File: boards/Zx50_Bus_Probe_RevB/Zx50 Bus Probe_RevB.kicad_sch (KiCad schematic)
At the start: 81 parts, among them J1 Zx50_EdgeConnector, J10 CH1, J11 CH2, J12 CH3, J13 DISPL SOCKET, J14 DISPL SOCKET, J15 Z80_Addr, J16 Z80_Data, J17 Z80_Ctrl, J18 Clock, J19 SH_Data, J2 OUT, J20 SH_Ctrl, J3 IN, J4 PIC PGM, J5 P0, J6 P1, J7 P2, J8 Send/Recv Card, J9 CH0, U1 MCP23S17_SP, U10 CD74HC4051E, U11 CD74HC4051E, U12 CD74HC4051E, U13 MCP23S17_SP, U14 CD74HC154M96, U15 OPA356xxD, U16 OPA356xxD, U17 PIC18F4620-I_P, U18 74AHCT541, U19 Jumper, U2 CD74HC4051E, U20 Jumper, U21 Jumper, U22 Jumper, U23 Jumper, U24 Jumper, U25 Jumper, U3 CD74HC4051E, U4 CD74HC4051E, U5 CD74HC4051E, U6 SN74ABT245BN, U7 SN74ABT245BN, U8 CD74HC4051E, U9 CD74HC4051E

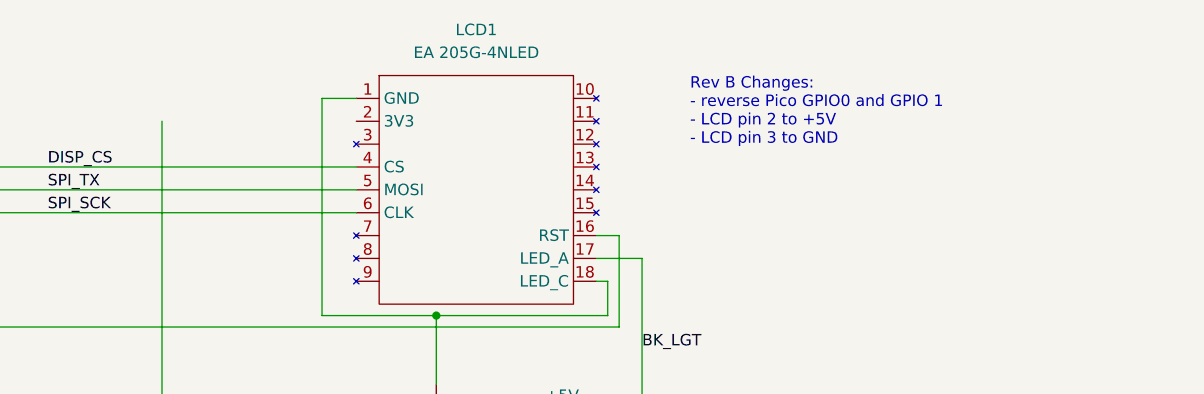
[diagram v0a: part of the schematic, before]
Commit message: enable wifi support for the bus probe
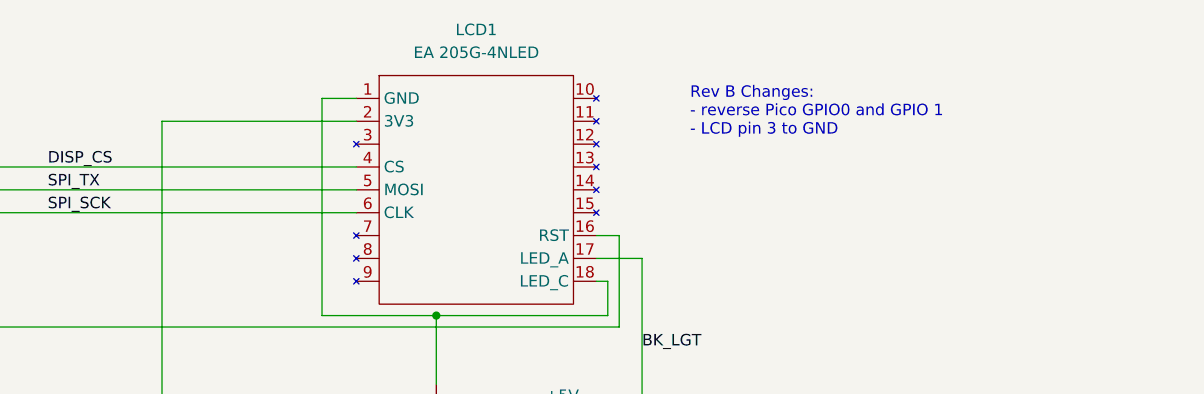
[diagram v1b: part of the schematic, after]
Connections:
- net at A1.36 (3V3): now also LCD1.2 (3V3)
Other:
- note added: "Rev B Changes: - reverse Pico GPIO0 and GPIO 1 - LCD pin 3 to GND"
- note removed: "Rev B Changes: - reverse Pico GPIO0 and GPIO 1 - LCD pin 2 to +5V - LCD pin 3 to GND"
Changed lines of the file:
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@@
 		)
 	)
-	(text "Rev B Changes:\n- reverse Pico GPIO0 and GPIO 1\n- LCD pin 2 to +5V\n- LCD pin 3 to GND"
+	(text "Rev B Changes:\n- reverse Pico GPIO0 and GPIO 1\n- LCD pin 3 to GND"
 		(exclude_from_sim yes)
 		(at 113.284 26.924 0)
@@
 		)
 		(stroke
+			(width 0)
+			(type default)
+		)
+	)
+	(wire
+		(pts
+			(xy 54.61 27.94) (xy 76.2 27.94)
+		)
+		(stroke

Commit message: Add extra banners and such to tcp server.  updates to revb bus probe.
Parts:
- added R20: 3.3K, Potentiometer_THT:Potentiometer_Runtron_RM-063_Horizontal, symbol Device:R_Potentiometer_Trim
- C21: value 10uF -> 47uF
- U10, U11, U12, U3, U4, U5, U8, U9: now fitted
- U15: renamed from U16; Digi-Key_PN 296-12407-5-ND -> 296-12407-5-ND
- U16: renamed from U15; Digi-Key_PN 296-12407-5-ND -> 296-12407-5-ND
- U2: Digi-Key_PN 296-12810-5-ND -> 296-12810-5-ND; now fitted
- renumbered C19 to C18, C18 to C19, C4 to C3, C3 to C4, J3 to J2, J2 to J3, U19 to J80, U20 to J81, U21 to J82, U22 to J83, U23 to J84, U24 to J85, U25 to J86, J13 to J90, J14 to J91
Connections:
- net +5V: now also A1.39 (VSYS)
- net GND: now also R20.1
- net PICO_TX: now reaches A1.1 (GPIO0), U18.2 (A0)
- net PICO_RX: now reaches A1.2 (GPIO1), R5.1, R6.2
- net at A1.36 (3V3), LCD1.2 (3V3): now also R20.3
- net at LCD1.3 (Contrast): now also R20.2
- no-connect marks 52 -> 51
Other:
- note added: "Rev B Changes: - reverse Pico GPIO0 and GPIO 1 - LCD pin 3 to contrast adjustment - Pico pin 39 (Vsys) to +5V"
- note removed: "Rev B Changes: - reverse Pico GPIO0 and GPIO 1 - LCD pin 3 to GND"
- moved on the sheet: J90, J91

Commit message: updates for more robust tcp handing.
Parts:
- renumbered J3 to J2, J2 to J3, U16 to U15, U15 to U16
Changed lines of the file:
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@@
 		(on_board yes)
 		(dnp no)
-		(property "Reference" "J2"
+		(property "Reference" "J3"
 			(at 120.65 336.8431 0)
 			(effects
@@
 			(project "Zx50 Bus Probe_RevB"
 				(path "/25f447e7-64bf-42d9-acfb-0aea4b7e6169"
-					(reference "J2")
+					(reference "J3")
 					(unit 1)
 				)
@@
 		(dnp no)
 		(fields_autoplaced yes)
-		(property "Reference" "U16"
+		(property "Reference" "U15"
 			(at 156.7881 302.26 0)
 			(effects
@@
 			(project ""
 				(path "/25f447e7-64bf-42d9-acfb-0aea4b7e6169"
-					(reference "U16")
+					(reference "U15")
 					(unit 1)
 				)
@@
 		(on_board yes)
 		(dnp no)
-		(property "Reference" "U15"
+		(property "Reference" "U16"
 			(at 144.526 350.52 0)
 			(effects
@@
 			(project "Zx50 Bus Probe_RevB"
 				(path "/25f447e7-64bf-42d9-acfb-0aea4b7e6169"
-					(reference "U15")
+					(reference "U16")
 					(unit 1)
 				)
@@
 		(on_board yes)
 		(dnp no)
-		(property "Reference" "J3"
+		(property "Reference" "J2"
 			(at 119.38 311.4431 0)
 			(effects
@@
 			(project ""
 				(path "/25f447e7-64bf-42d9-acfb-0aea4b7e6169"
-					(reference "J3")
+					(reference "J2")
 					(unit 1)
 				)

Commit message: Many updates and board revisions.
- Backplane Rev D for better AC termination.
- BusProbe revision, much smaller card, use surface mount, faster multiplexers.
- Revised clock mezzanine to reduce ringing.
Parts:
- removed D1: MCLK, LED_THT:LED_D5.0mm_Horizontal_O1.27mm_Z3.0mm, symbol Device:LED
- removed D2: CLK, LED_THT:LED_D5.0mm_Horizontal_O1.27mm_Z3.0mm, symbol Device:LED
- removed J18: Clock, zx50_footprints:PinHeader_2x02_P2.54mm_Vertical_Row_Letter_Last, symbol Connector_Generic:Conn_02x02_Row_Letter_Last
- removed R7, R8: 2.2K, Resistor_THT:R_Axial_DIN0207_L6.3mm_D2.5mm_P5.08mm_Vertical, symbol Device:R
- removed U1, U13: MCP23S17_SP, Package_DIP:DIP-28_W7.62mm_Socket, symbol Interface_Expansion:MCP23S17_SP
- removed U10, U11, U12, U2, U3, U4, U5, U8, U9: CD74HC4051E, Package_DIP:DIP-16_W7.62mm_Socket, symbol 74xx:74HC4051
- removed U17: PIC18F4620-I_P, Package_DIP:DIP-40_W15.24mm_Socket, symbol zx50_symbols:PIC18F4620-I_P
- added C22, C23, C24, C25: .1uF, Capacitor_SMD:C_0805_2012Metric, symbol Device:C_Small
- added D4: 1N4001, Diode_THT:D_DO-41_SOD81_P10.16mm_Horizontal, symbol Diode:1N4001
- added D5: PIC, LED_THT:LED_D5.0mm_Horizontal_O1.27mm_Z3.0mm, symbol Device:LED
- added R11: 470, Resistor_THT:R_Axial_DIN0207_L6.3mm_D2.5mm_P5.08mm_Vertical, symbol Device:R
- added U1, U13, U21: MCP23S17_SO, Package_SO:SOIC-28W_7.5x17.9mm_P1.27mm, symbol Interface_Expansion:MCP23S17_SO
- added U10, U11, U12, U2, U3, U4, U5, U8, U9: 74CBT3251, Package_SO:SOIC-16_3.9x9.9mm_P1.27mm, symbol zx50_symbols:SN74CBT3251DR
- added U17, U19, U22, U23: SN74ABT245BN, zx50_footprints:NS20, symbol zx50_symbols:SN74ABT245BN
- added U20: PIC18F27Q43-I/SO, zx50_footprints:SOIC28_SO_MCH, symbol zx50_symbols:PIC18F27Q43-I_SO
- C1, C10, C11, C12, C13, C14, C15, C16, C17, C18, C19, C2, C20, C3, C4, C5, C6, C7, C8, C9: footprint Capacitor_THT:C_Disc_D5.0mm_W2.5mm_P2.50mm -> Capacitor_SMD:C_0805_2012Metric
- R2: footprint Resistor_THT:R_Axial_DIN0207_L6.3mm_D2.5mm_P10.16mm_Horizontal -> Resistor_SMD:R_0805_2012Metric_Pad1.20x1.40mm_HandSolder
- U18: footprint Package_DIP:DIP-20_W7.62mm_Socket -> Package_SO:SOIC-20W_7.5x12.8mm_P1.27mm; Digi-Key_PN 296-4755-5-ND -> 296-4754-1-ND
- U6, U7: footprint Package_DIP:DIP-20_W7.62mm_Socket -> zx50_footprints:NS20; Digi-Key_PN 296-3970-5-ND -> 296-15879-1-ND
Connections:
- net +5V: now also C20.1, C22.1, C23.1, C24.1, C25.1, D4.2 (A), D5.2 (A), U1.9 (VDD), U10.16 (VCC), U11.16 (VCC), U12.16 (VCC), U13.15 (A0), U13.9 (VDD), U17.20 (VCC), U19.20 (VCC), U2.16 (VCC), U20.20 (VDD), U21.16 (A1), U21.9 (VDD), U22.20 (VCC), U23.20 (VCC), U3.16 (VCC), U4.16 (VCC), U5.16 (VCC), U8.16 (VCC), U9.16 (VCC); no longer A1.39 (VSYS), C20.2
- net A0: now also U17.2 (A1), U4.12 (B8); no longer J15.1b (Pin_1b)
- net A1: now also U17.3 (A2), U4.4 (B1); no longer J15.2b (Pin_2b)
- net A10: now also U19.4 (A3), U5.13 (B7); no longer J15.11b (Pin_11b)
- net A11: now also U19.5 (A4), U5.3 (B2); no longer J15.12b (Pin_12b)
- net A12: now also U19.6 (A5), U5.14 (B6); no longer J15.13b (Pin_13b)
- net A13: now also U19.7 (A6), U5.2 (B3); no longer J15.14b (Pin_14b)
- net A14: now also U19.8 (A7), U5.15 (B5); no longer J15.15b (Pin_15b)
- net A15: now also U19.9 (A8), U5.1 (B4); no longer J15.16b (Pin_16b)
- net A2: now also U17.4 (A3), U4.13 (B7); no longer J15.3b (Pin_3b)
- net A3: now also U17.5 (A4), U4.3 (B2); no longer J15.4b (Pin_4b)
- net A4: now also U17.6 (A5), U4.14 (B6); no longer J15.5b (Pin_5b)
- net A5: now also U17.7 (A6), U4.2 (B3); no longer J15.6b (Pin_6b)
- net A6: now also U17.8 (A7), U4.15 (B5); no longer J15.7b (Pin_7b)
- net A7: now also U17.9 (A8), U4.1 (B4); no longer J15.8b (Pin_8b)
- net A8: now also U19.2 (A1), U5.12 (B8); no longer J15.9b (Pin_9b)
- net A9: now also U19.3 (A2), U5.4 (B1); no longer J15.10b (Pin_10b)
- net AN: now also U10.5 (A), U11.5 (A), U12.5 (A), U2.5 (A), U3.5 (A), U4.5 (A), U5.5 (A), U8.5 (A), U9.5 (A)
- net AUX: now also U20.25 (RB4)
- net CHIP0: now also U18.12 (Y6); no longer U18.17 (Y1)
- net CHIP1: now also U18.13 (Y5); no longer U18.16 (Y2)
- net CHIP2: now also U18.14 (Y4); no longer U18.15 (Y3)
- net CHIP3: now also U18.15 (Y3); no longer U18.14 (Y4)
- net CLK: now also U20.12 (RC1), U9.13 (B7)
- net D0: now also U3.12 (B8); no longer J16.1b (Pin_1b)
- net D1: now also U3.4 (B1); no longer J16.2b (Pin_2b)
- net D2: now also U3.13 (B7); no longer J16.3b (Pin_3b)
- net D3: now also U3.3 (B2); no longer J16.4b (Pin_4b)
- net D4: now also U3.14 (B6); no longer J16.5b (Pin_5b)
- net D5: now also U3.2 (B3); no longer J16.6b (Pin_6b)
- net D6: now also U3.15 (B5); no longer J16.7b (Pin_7b)
- net D7: now also U3.1 (B4); no longer J16.8b (Pin_8b)
- net G0: now also U11.4 (B1)
- net G1: now also U11.12 (B8)
- net G10: now also U12.3 (B2)
- net G11: now also U12.13 (B7)
- net G12: now also U12.2 (B3), U23.9 (A8)
- net G13: now also U12.14 (B6)
- net G14: now also U12.1 (B4), U23.7 (A6)
- net G15: now also U7.9 (A8), U12.15 (B5)
- net G2: now also U11.3 (B2)
- net G3: now also U11.13 (B7)
- net G4: now also U11.2 (B3)
- net G5: now also U11.14 (B6)
- net G6: now also U11.1 (B4)
- net G7: now also U11.15 (B5)
- net G8: now also U12.4 (B1)
- net G9: now also U12.12 (B8)
- net GND: now also C20.2, C22.2, C23.2, C24.2, C25.2, U1.10 (VSS), U1.15 (A0), U1.16 (A1), U1.17 (A2), U10.8 (GND), U11.8 (GND), U12.8 (GND), U13.10 (VSS), U13.16 (A1), U13.17 (A2), U17.10 (GND), U19.10 (GND), U2.8 (GND), U20.19 (VSS), U20.8 (VSS), U21.10 (VSS), U21.15 (A0), U21.17 (A2), U22.10 (GND), U23.10 (GND), U3.8 (GND), U4.8 (GND), U5.8 (GND), U8.8 (GND), U9.8 (GND); no longer C20.1
- net IEI: now also U9.4 (B1)
- net IEO: now also U9.3 (B2)
- net MCLK: now also U20.13 (RC2), U9.12 (B8)
- net MCLR_N: now also U20.1 (MCLR/VPP/RE3)
- net PGC: now also U20.27 (RB6/ICSPCLK)
- net PGD: now also U20.28 (RB7/ICSPDAT)
- net PICO_TX: now also U18.9 (A7); no longer U18.2 (A0)
- net PORT0: now also U18.16 (Y2), U10.11 (S0), U11.11 (S0), U12.11 (S0), U2.11 (S0), U3.11 (S0), U4.11 (S0), U5.11 (S0), U8.11 (S0), U9.11 (S0); no longer U18.13 (Y5)
- net PORT1: now also U18.17 (Y1), U10.10 (S1), U11.10 (S1), U12.10 (S1), U2.10 (S1), U3.10 (S1), U4.10 (S1), U5.10 (S1), U8.10 (S1), U9.10 (S1); no longer U18.12 (Y6)
- net PORT2: now also U18.18 (Y0), U10.9 (S2), U11.9 (S2), U12.9 (S2), U2.9 (S2), U3.9 (S2), U4.9 (S2), U5.9 (S2), U8.9 (S2), U9.9 (S2); no longer U18.11 (Y7)
- net RA0: now also U6.19 (*OE), U20.2 (RA0); no longer U7.19 (*OE)
- net RA1: now also U6.1 (DIR), U20.3 (RA1); no longer U7.1 (DIR)
- net RA2: now also U7.19 (*OE), U17.19 (*OE), U19.19 (*OE), U20.4 (RA2); no longer U6.19 (*OE)
- net RA3: now also U7.1 (DIR), U17.1 (DIR), U19.1 (DIR), U20.5 (RA3); no longer U6.1 (DIR)
- net RA4: now also U1.18 (~{RESET}), U13.18 (~{RESET}), U20.6 (RA4), U21.18 (~{RESET})
- net RA5: now also U1.11 (~{CS}), U13.11 (~{CS}), U20.7 (RA5), U21.11 (~{CS})
- net RB5: now also R11.1, U20.26 (RB5); no longer J4.6 (Pin_6), U7.18 (B1)
- net RX: now also U18.11 (Y7), U20.18 (RC7); no longer U18.18 (Y0)
- net SCK: now also U1.12 (SCK), U13.12 (SCK), U20.14 (RC3), U21.12 (SCK)
- net SD0: now also U10.12 (B8), U22.2 (A1); no longer J19.1b (Pin_1b)
- net SD1: now also U10.4 (B1), U22.3 (A2); no longer J19.2b (Pin_2b)
- net SD2: now also U10.13 (B7), U22.4 (A3); no longer J19.3b (Pin_3b)
- net SD3: now also U10.3 (B2), U22.5 (A4); no longer J19.4b (Pin_4b)
- net SD4: now also U10.14 (B6), U22.6 (A5); no longer J19.5b (Pin_5b)
- net SD5: now also U10.2 (B3), U22.7 (A6); no longer J19.6b (Pin_6b)
- net SD6: now also U10.15 (B5), U22.8 (A7); no longer J19.7b (Pin_7b)
- net SD7: now also U10.1 (B4), U22.9 (A8); no longer J19.8b (Pin_8b)
- net SDI: now also U1.14 (SO), U13.14 (SO), U20.15 (RC4), U21.14 (SO)
- net SDO: now also U1.13 (SI), U13.13 (SI), U20.16 (RC5), U21.13 (SI)
- net SEL0: now also U3.7 (*OE)
- net SEL1: now also U2.7 (*OE)
- net SEL2: now also U12.7 (*OE)
- net SEL3: now also U11.7 (*OE)
- net SEL4: now also U4.7 (*OE)
- net SEL5: now also U5.7 (*OE)
- net SEL6: now also U10.7 (*OE)
- net SEL7: now also U8.7 (*OE)
- net SEL8: now also U9.7 (*OE)
- net SH_RW: now also U23.5 (A4), U9.1 (B4); no longer J20.4b (Pin_4b)
- net TX: now also U20.17 (RC6)
- net ~BUSAK~: now also U7.8 (A7), U8.15 (B5)
- net ~BUSRQ~: now also U20.24 (RB3), U8.2 (B3)
- net ~HALT~: now also U8.13 (B7)
- net ~INT~: now also U20.21 (RB0), U8.1 (B4)
- net ~IORQ~: now also U2.3 (B2); no longer J17.4b (Pin_4b)
- net ~M1~: now also U2.14 (B6); no longer J17.5b (Pin_5b)
- net ~MREQ~: now also U2.13 (B7); no longer J17.3b (Pin_3b)
- net ~NMI~: now also U2.1 (B4)
- net ~RD~: now also U2.12 (B8); no longer J17.1b (Pin_1b)
- net ~RESET~: now also U8.4 (B1); no longer J17.7b (Pin_7b)
- net ~RFSH~: now also U2.2 (B3)
- net ~SH_BUSY~: now also U20.23 (RB2), U8.14 (B6)
- net ~SH_DONE~: now also U23.6 (A5), U8.3 (B2); no longer J20.5b (Pin_5b)
- net ~SH_EN~: now also U23.4 (A3), U9.15 (B5); no longer J20.1b (Pin_1b)
- net ~SH_INC~: now also U23.3 (A2), U9.2 (B3); no longer J20.3b (Pin_3b)
- net ~SH_STB~: now also U23.2 (A1), U9.14 (B6); no longer J20.2b (Pin_2b)
- net ~WAIT~: now also U2.15 (B5), U20.22 (RB1)
- net ~WR~: now also U2.4 (B1); no longer J17.2b (Pin_2b)
- net at A1.9 (GPIO6), J5.3 (Pin_3): now also U18.4 (A2); no longer U18.7 (A5)
- net at A1.5 (GPIO3), J10.3 (Pin_3): now also U18.7 (A5); no longer U18.4 (A2)
- net at A1.11 (GPIO8), J7.3 (Pin_3): now also U18.2 (A0); no longer U18.9 (A7)
- net at A1.7 (GPIO5), J12.3 (Pin_3): now also U18.5 (A3); no longer U18.6 (A4)
- net at A1.4 (GPIO2), J9.3 (Pin_3): now also U18.8 (A6); no longer U18.3 (A1)
- net at A1.6 (GPIO4), J11.3 (Pin_3): now also U18.6 (A4); no longer U18.5 (A3)
- net at A1.10 (GPIO7), J6.3 (Pin_3): now also U18.3 (A1); no longer U18.8 (A6)
- net AN_IN: now reaches J3.1 (In), R1.2, U16.3 (+)
- net AN_OUT: now reaches R2.2, U15.2 (-), U15.6
- net DISP_RST: now reaches A1.26 (GPIO20), LCD1.16 (RST)
- net PIC_PICO_INT: now reaches A1.27 (GPIO21)
- net PIC_PICO_INT: now also U20.11 (RC0)
- net X.G15: now reaches U7.11 (B8)
- net X.G15: now also U21.8 (GPB7)
- net X.~BUSAK~: now reaches U7.12 (B7)
- net X.~BUSAK~: now also U21.7 (GPB6)
- net OUT: now reaches J2.1 (In), R2.1
- net RB3 renamed X.~MREQ~
- net X.~MREQ~: now also J17.3b (Pin_3b), U21.3 (GPB2)
- net RB4 renamed X.~IORQ~
- net X.~IORQ~: now also J17.4b (Pin_4b), U21.4 (GPB3)
- net RD0 renamed X.D0
- net X.D0: now also J16.1b (Pin_1b), U21.28 (GPA7)
- net RD1 renamed X.D1
- net X.D1: now also J16.2b (Pin_2b), U21.27 (GPA6)
- net RD2 renamed X.D2
- net X.D2: now also J16.3b (Pin_3b), U21.26 (GPA5)
- net RD3 renamed X.D3
- net X.D3: now also J16.4b (Pin_4b), U21.25 (GPA4)
- net RD4 renamed X.D4
- net X.D4: now also J16.5b (Pin_5b), U21.24 (GPA3)
- net RD5 renamed X.D5
- net X.D5: now also J16.6b (Pin_6b), U21.23 (GPA2)
- net RD6 renamed X.D6
- net X.D6: now also J16.7b (Pin_7b), U21.22 (GPA1)
- net RD7 renamed X.D7
- net X.D7: now also J16.8b (Pin_8b), U21.21 (GPA0)
- net RE0 renamed X.~WR~
- net X.~WR~: now also J17.2b (Pin_2b), U21.2 (GPB1)
- net RE1 renamed X.~M1~
- net X.~M1~: now also J17.5b (Pin_5b), U21.5 (GPB4)
- net RE2 renamed X.~RESET~
- net X.~RESET~: now also J17.7b (Pin_7b), U21.6 (GPB5)
- new net: D5.1 (K), R11.2
- new net: A1.39 (VSYS), D4.1 (K)
- new net RA6: U20.10 (RA6), U22.19 (*OE), U23.19 (*OE)
- new net RA7: U20.9 (RA7), U22.1 (DIR), U23.1 (DIR)
- new net X.A0: J15.1b (Pin_1b), U1.21 (GPA0), U17.18 (B1)
- new net X.A1: J15.2b (Pin_2b), U1.22 (GPA1), U17.17 (B2)
- new net X.A10: J15.11b (Pin_11b), U1.3 (GPB2), U19.16 (B3)
- new net X.A11: J15.12b (Pin_12b), U1.4 (GPB3), U19.15 (B4)
- new net X.A12: J15.13b (Pin_13b), U1.5 (GPB4), U19.14 (B5)
- new net X.A13: J15.14b (Pin_14b), U1.6 (GPB5), U19.13 (B6)
- new net X.A14: J15.15b (Pin_15b), U1.7 (GPB6), U19.12 (B7)
- new net X.A15: J15.16b (Pin_16b), U1.8 (GPB7), U19.11 (B8)
- new net X.A2: J15.3b (Pin_3b), U1.23 (GPA2), U17.16 (B3)
- new net X.A3: J15.4b (Pin_4b), U1.24 (GPA3), U17.15 (B4)
- new net X.A4: J15.5b (Pin_5b), U1.25 (GPA4), U17.14 (B5)
- new net X.A5: J15.6b (Pin_6b), U1.26 (GPA5), U17.13 (B6)
- new net X.A6: J15.7b (Pin_7b), U1.27 (GPA6), U17.12 (B7)
- new net X.A7: J15.8b (Pin_8b), U1.28 (GPA7), U17.11 (B8)
- new net X.A8: J15.9b (Pin_9b), U1.1 (GPB0), U19.18 (B1)
- new net X.A9: J15.10b (Pin_10b), U1.2 (GPB1), U19.17 (B2)
- new net X.G12: U13.28 (GPA7), U23.11 (B8)
- new net X.G14: U13.26 (GPA5), U23.13 (B6)
- new net X.SD0: J19.1b (Pin_1b), U13.1 (GPB0), U22.18 (B1)
- new net X.SD1: J19.2b (Pin_2b), U13.2 (GPB1), U22.17 (B2)
- new net X.SD2: J19.3b (Pin_3b), U13.3 (GPB2), U22.16 (B3)
- new net X.SD3: J19.4b (Pin_4b), U13.4 (GPB3), U22.15 (B4)
- new net X.SD4: J19.5b (Pin_5b), U13.5 (GPB4), U22.14 (B5)
- new net X.SD5: J19.6b (Pin_6b), U13.6 (GPB5), U22.13 (B6)
- new net X.SD6: J19.7b (Pin_7b), U13.7 (GPB6), U22.12 (B7)
- new net X.SD7: J19.8b (Pin_8b), U13.8 (GPB7), U22.11 (B8)
- new net X.SH_RW: J20.4b (Pin_4b), U13.24 (GPA3), U23.15 (B4)
- new net X.~RD~: J17.1b (Pin_1b), U21.1 (GPB0), U7.18 (B1)
- new net X.~SH_DONE~: J20.5b (Pin_5b), U13.25 (GPA4), U23.14 (B5)
- new net X.~SH_EN~: J20.3b (Pin_3b), U13.23 (GPA2), U23.16 (B3)
- new net X.~SH_INC~: J20.2b (Pin_2b), U13.22 (GPA1), U23.17 (B2)
- new net X.~SH_STB~: J20.1b (Pin_1b), U13.21 (GPA0), U23.18 (B1)
- no-connect marks 51 -> 49
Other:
- moved on the sheet: C12, C18, C2, C20, D3, J15, J16, J17, J19, J2, J20, J4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

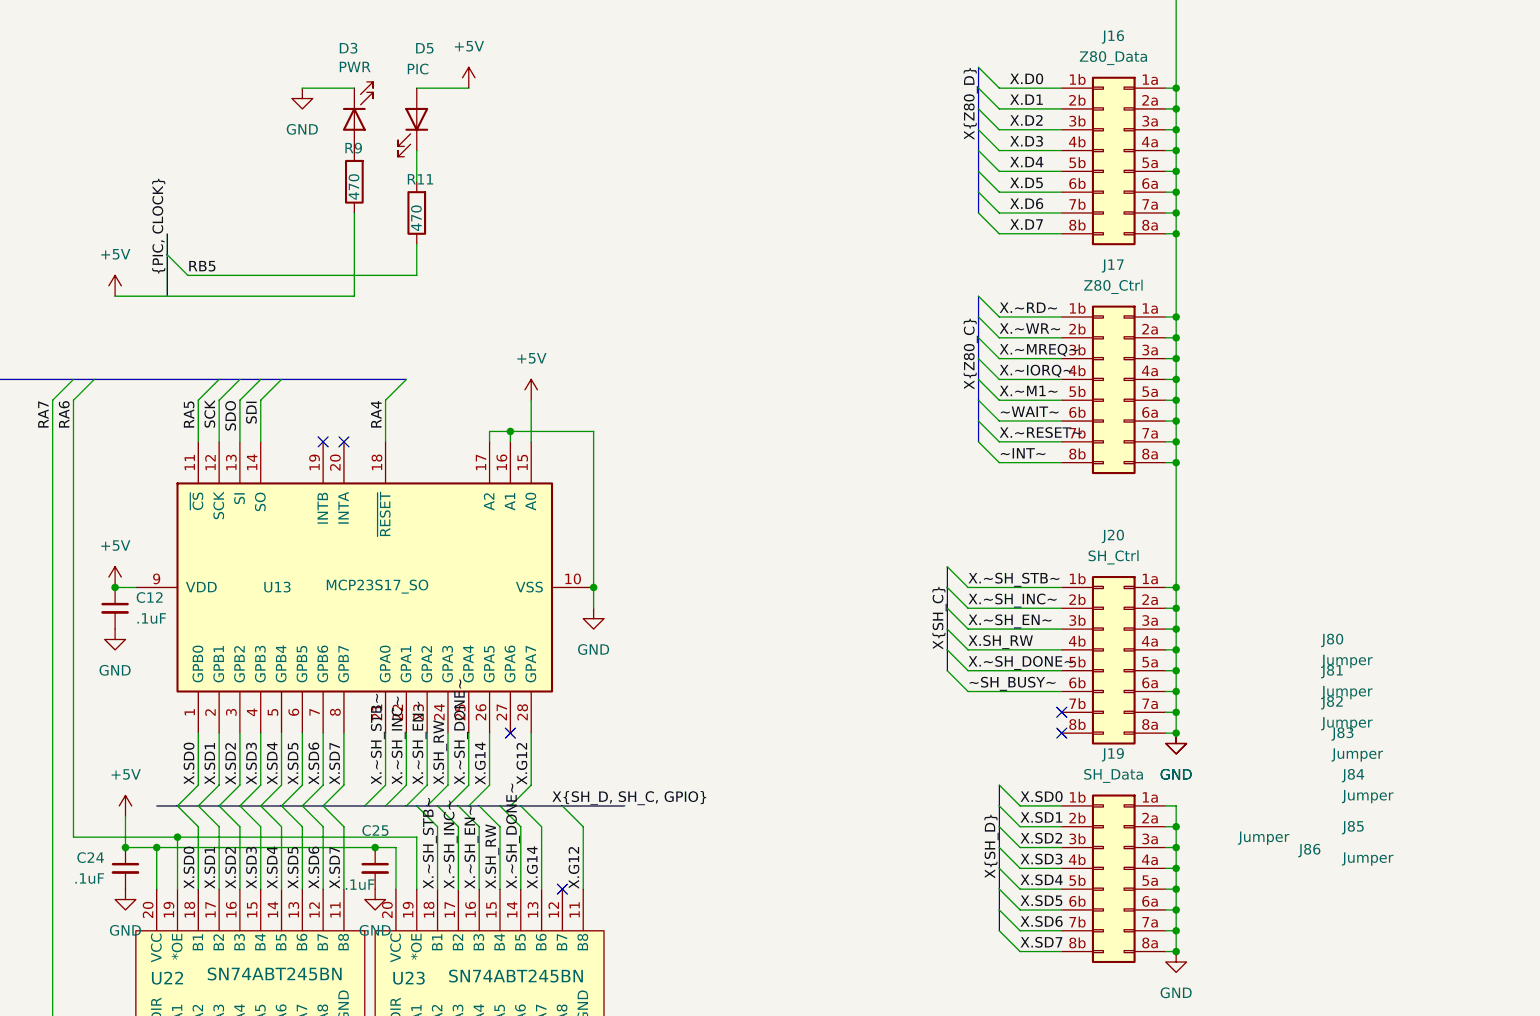
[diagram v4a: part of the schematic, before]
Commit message: Lots of updates: Work on memory card Rev C with Lattice XO3LF, finish up the front panel card firmware for the pico., add some results for the clock mezzanine Rev B.
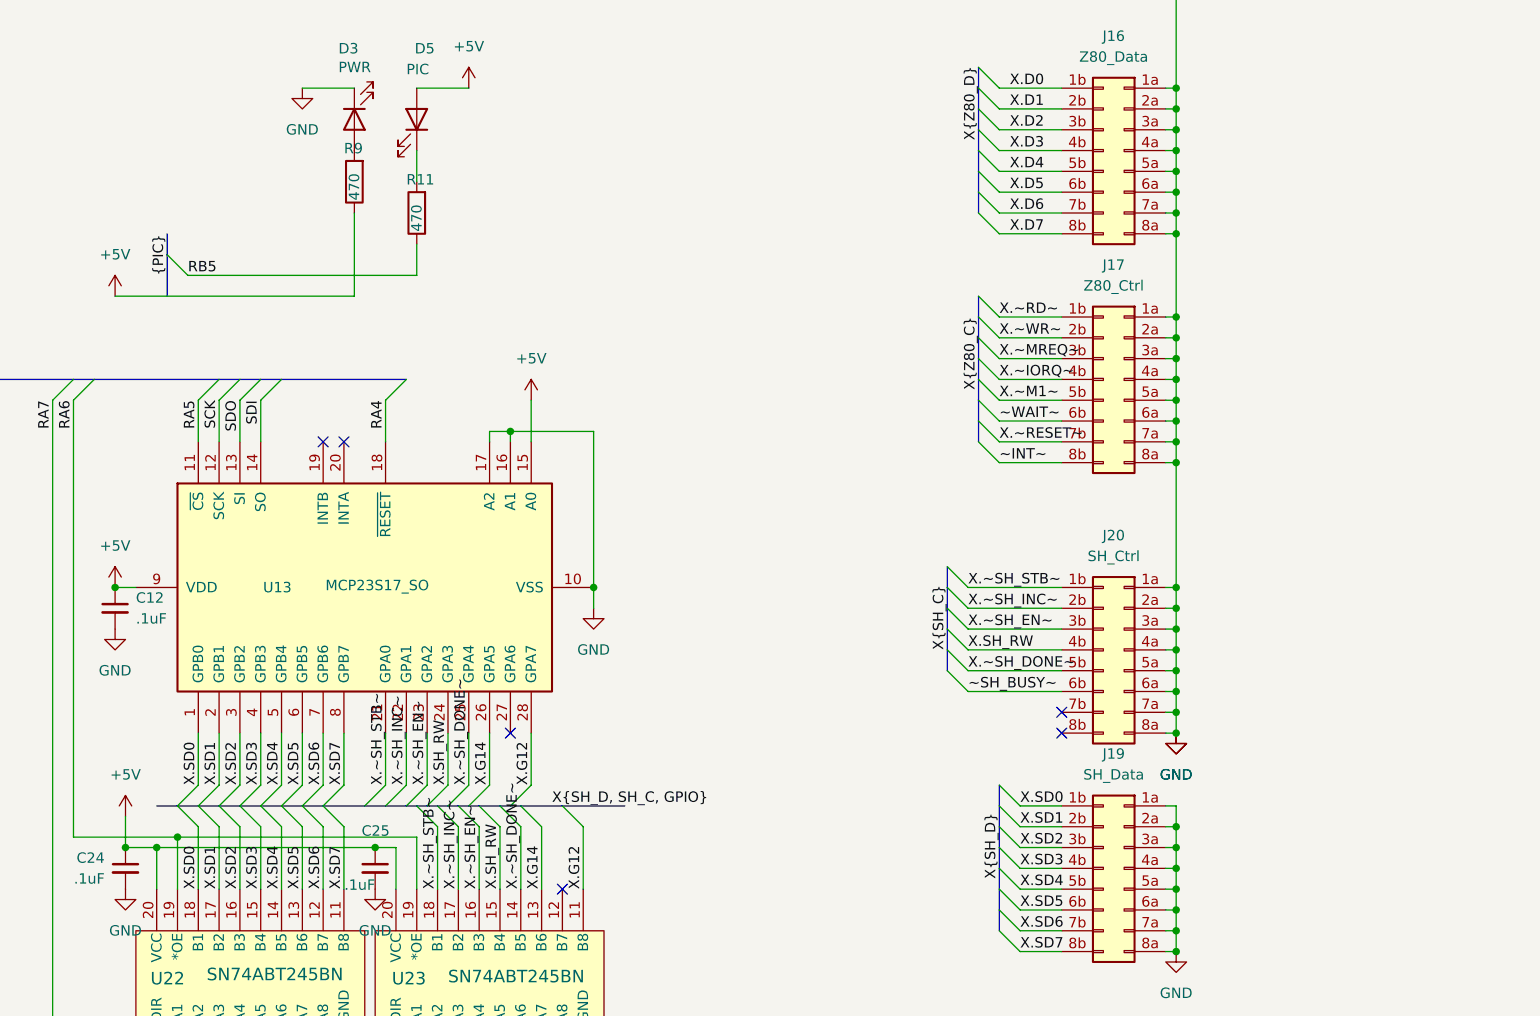
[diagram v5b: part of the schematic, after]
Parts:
- removed J80, J81, J82, J83, J84, J85, J86: Jumper, symbol Jumper:Jumper_1
- A1: Digi-Key_PN SC1634 -> (none); DigiKey_PN (none) -> SC1634; now left out of the parts list
- C1, C10, C11, C12, C13, C14, C15, C16, C17, C18, C19, C2, C20, C21, C22, C23, C24, C25, C3, C4, C5, C6, C7, C8, C9, D4, R10, R11, R20, R3, R4, R5, R6, R9: now left out of the parts list
- D3, D5: Digi-Key_PN 732-5016-ND -> (none); DigiKey_PN (none) -> 732-5016-ND; now left out of the parts list
- J1: Digi-Key_PN 2057-PH2RA-80-UA-ND -> (none); DigiKey_PN (none) -> 2057-PH2RA-80-UA-ND; now left out of the parts list
- J10, J11, J12, J5, J6, J7, J9: Digi-Key_PN 732-5316-ND -> (none); DigiKey_PN (none) -> 732-5316-ND; now left out of the parts list
- J15: Digi-Key_PN 732-5307-ND -> (none); DigiKey_PN (none) -> 732-5307-ND; now left out of the parts list
- J16, J17, J19, J20: Digi-Key_PN 732-5299-ND -> (none); DigiKey_PN (none) -> 732-5299-ND; now left out of the parts list
- J2, J3: Digi-Key_PN ARF1060-ND -> (none); DigiKey_PN (none) -> ARF1060-ND; now left out of the parts list
- J4: Digi-Key_PN 732-5339-ND -> (none); DigiKey_PN (none) -> 732-5339-ND; now left out of the parts list
- J8: Digi-Key_PN 732-2098-ND -> (none); DigiKey_PN (none) -> 732-2098-ND; now left out of the parts list
- J90, J91: Digi-Key_PN S5751-09-ND -> (none); DigiKey_PN (none) -> S5751-09-ND; now left out of the parts list
- LCD1: Digi-Key_PN 1481-EADIP205G-4NLED-ND -> (none); DigiKey_PN (none) -> 1481-EADIP205G-4NLED-ND; now left out of the parts list
- R1, R2: Digi-Key_PN 541-CPF149R900FKRE6CT-ND -> (none); DigiKey_PN (none) -> 541-CPF149R900FKRE6CT-ND; now left out of the parts list
- U1, U13, U21: DigiKey_PN (none) -> MCP23S17-E/SO-ND; SKU (none) -> MCP23S17-E/SO
- U10, U11, U12, U2, U3, U4, U5, U8, U9: DigiKey_PN (none) -> 296-49883-1-ND; SKU (none) -> SN74CBT3251DR
- U14: Digi-Key_PN 296-24352-1-ND -> (none); DigiKey_PN (none) -> 296-24352-1-ND
- U15, U16: Digi-Key_PN 296-12407-5-ND -> (none); DigiKey_PN (none) -> 296-12407-5-ND
- U17, U19, U6, U7: Digi-Key_PN 296-15879-1-ND -> (none); DigiKey_PN (none) -> 296-15879-1-ND
- U18: Digi-Key_PN 296-4754-1-ND -> (none); DigiKey_PN (none) -> 296-4754-1-ND
- U22, U23: Digi-Key_PN 296-3970-5-ND -> (none); DigiKey_PN (none) -> 296-15879-1-ND

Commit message: reorg firmware
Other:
- note added: "Only populate one direction"
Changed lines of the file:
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@@
+		)
+	)
+	(text "Only populate one direction"
+		(exclude_from_sim no)
+		(at 144.78 359.41 0)
+		(effects
+			(font
+				(size 1.27 1.27)
+			)
 		)
 	)
